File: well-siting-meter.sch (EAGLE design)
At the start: 27 parts, among them J2 7805

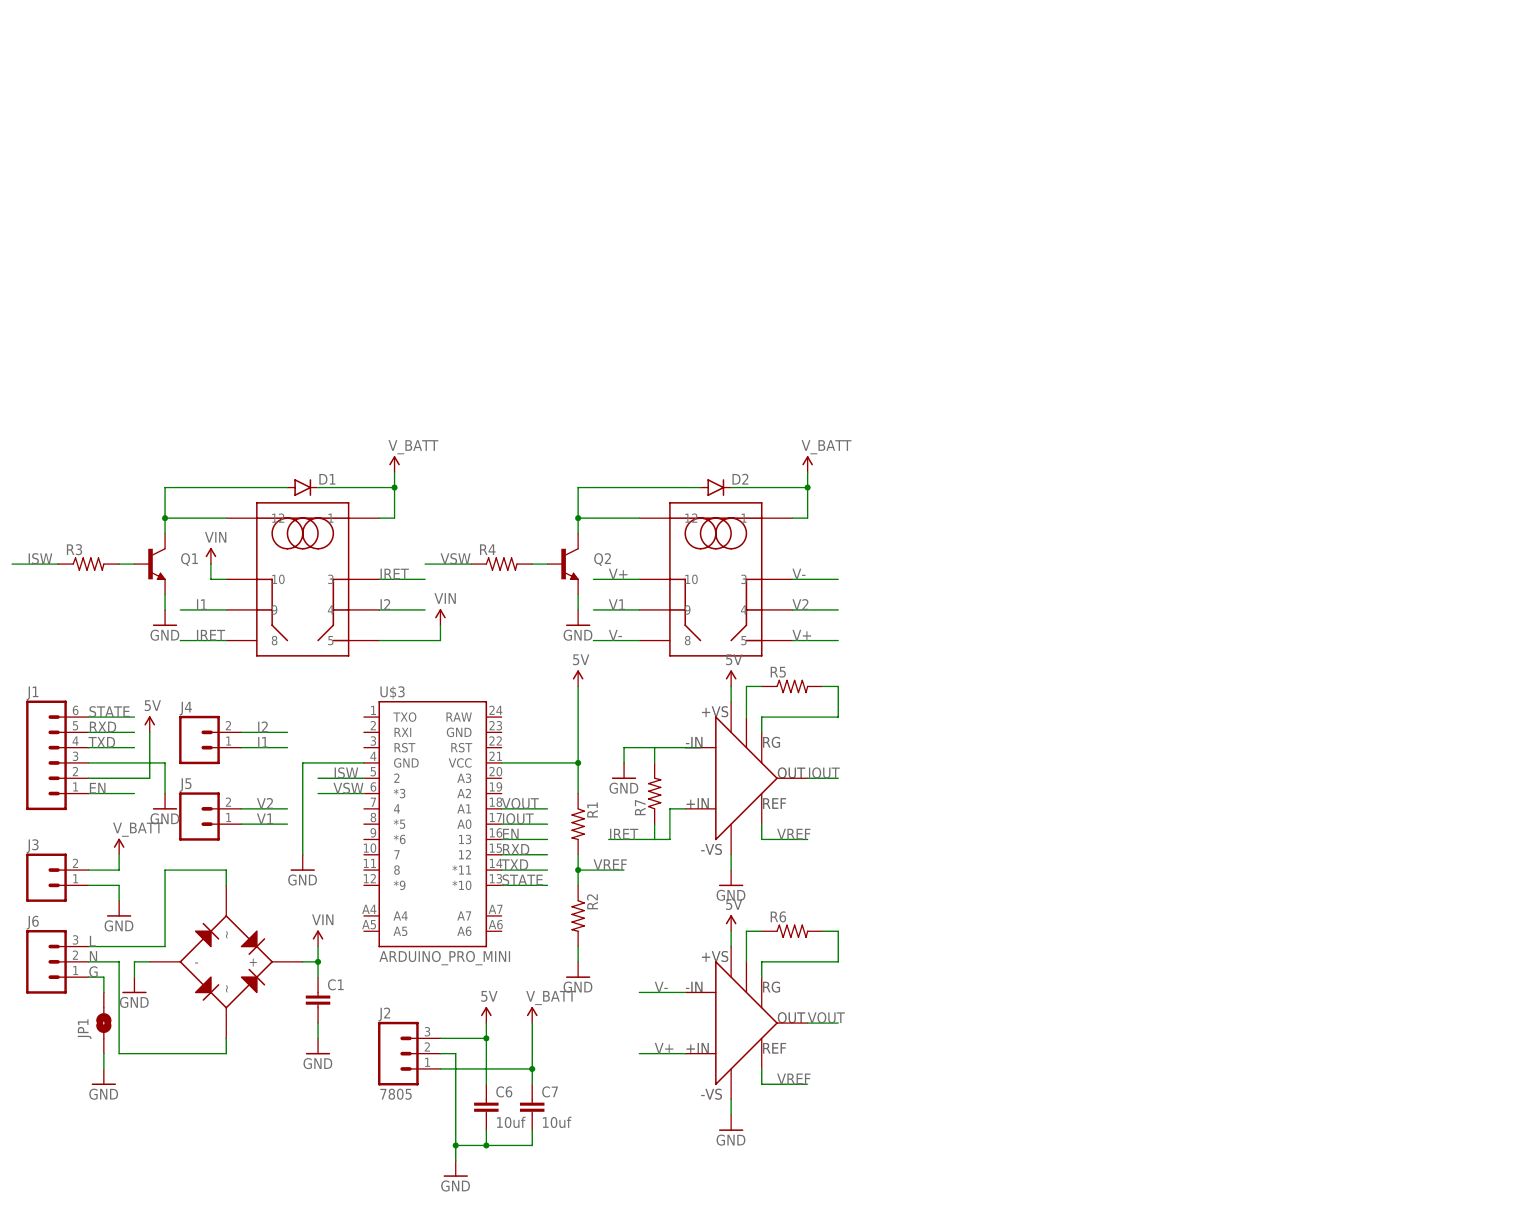
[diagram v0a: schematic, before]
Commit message: boost circuit, lcd screen, starting board layout
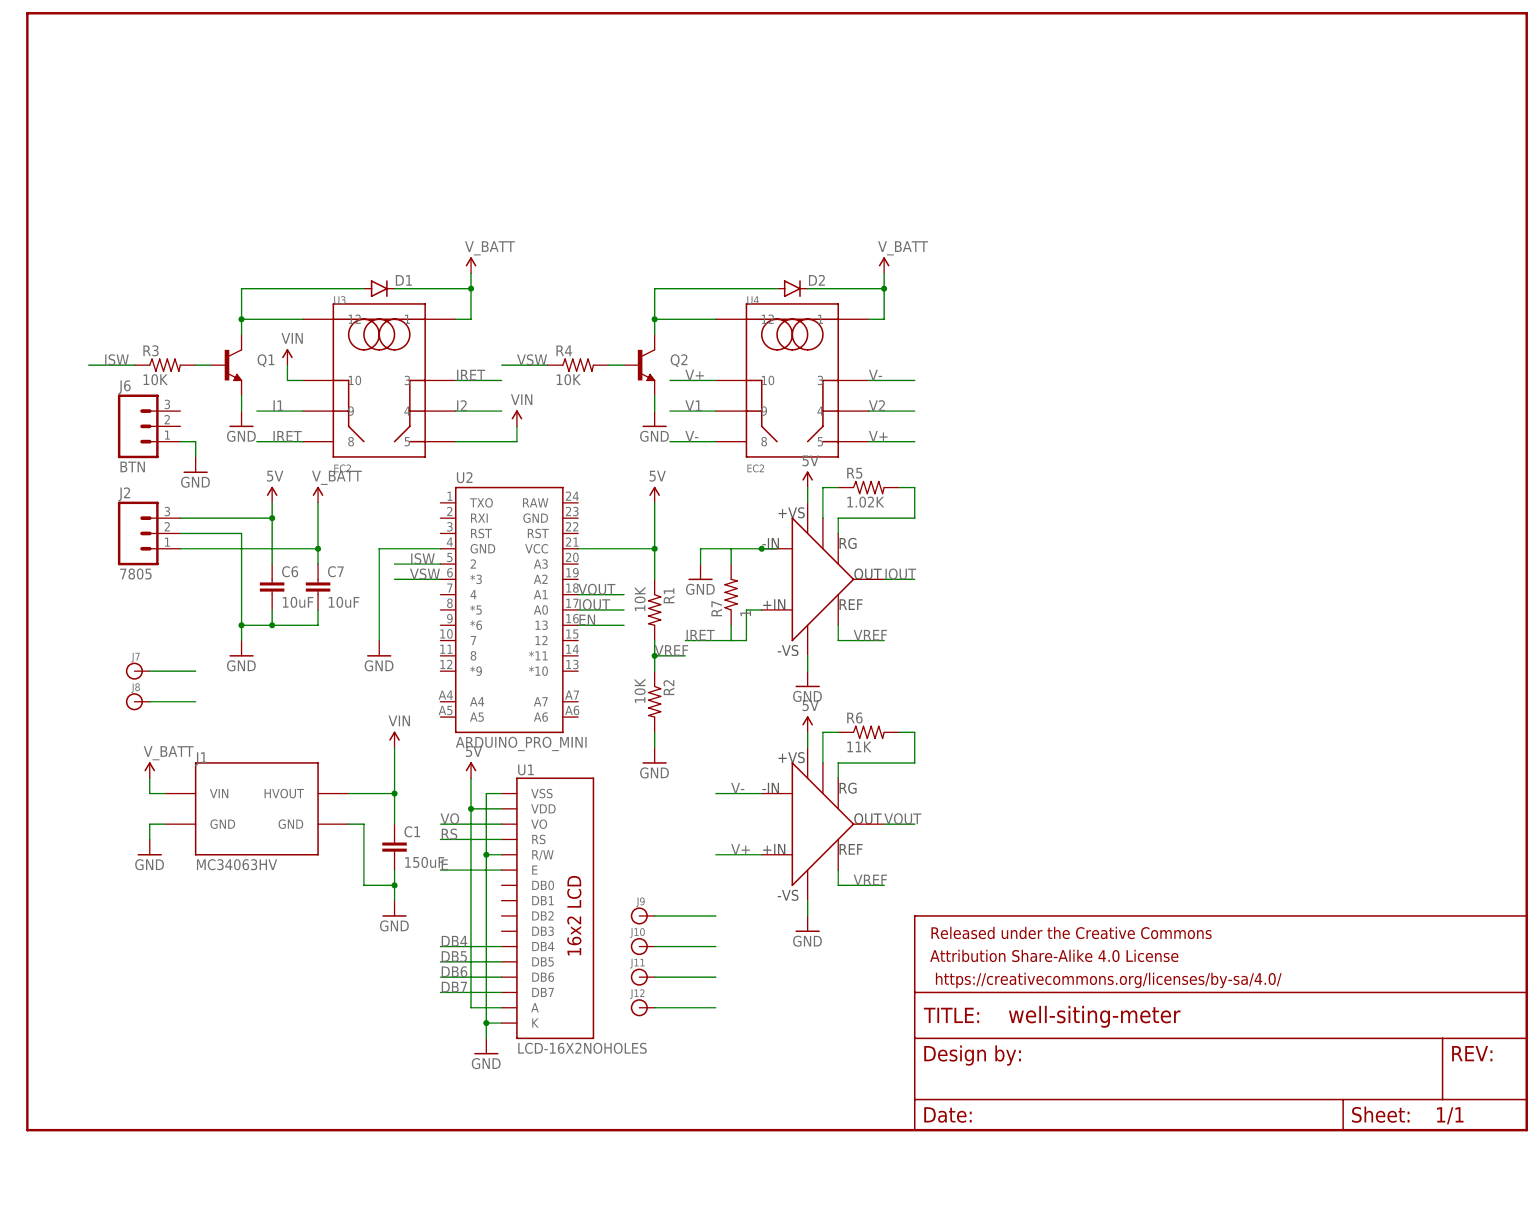
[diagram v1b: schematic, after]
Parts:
- removed J3, J4, J5: (no value), SparkFun-Connectors:M025MM
- removed JP1: JUMPER-PAD-2-NO, SparkFun-Passives:JUMPER-PAD-2-NO
- removed U$1, U$2: EC2, ec2:EC2
- removed U$3: ARDUINO_PRO_MINI, SparkFun-Boards:ARDUINO_PRO_MINI
- removed U$4, U$5: AD623, ad623:AD623
- removed U$6: DF2X, df2x:DF2X
- added FRAME1: FRAME-LETTER, SparkFun-Aesthetics:FRAME-LETTER
- added J10, J11, J12, J7, J8, J9: (no value), SparkFun-Connectors:BANANA_CONN
- added U1: LCD-16X2NOHOLES, SparkFun-Displays:LCD-16X2NOHOLES
- added U2: ARDUINO_PRO_MINI, SparkFun-Boards:ARDUINO_PRO_MINI
- added U3, U4: EC2, ec2:EC2
- added U5, U6: AD623, ad623:AD623
- C1: value (none) -> 150uF
- C6, C7: value 10uf -> 10uF
- J1: value (none) -> MC34063HV; device SparkFun-Connectors:M06SILK_FEMALE_PTH -> mc34063hv:MC34063HV
- J6: value (none) -> BTN; device SparkFun-Connectors:M03-SCREW-5MM -> SparkFun-Connectors:M03PTH; PN (none) -> 811-2196-5-ND; PN2 (none) -> LM7805CT-ND
- R1, R2, R3, R4: value (none) -> 10K
- R5: value (none) -> 1.02K
- R6: value (none) -> 11K
- R7: value (none) -> 1
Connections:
- removed net G: J6.1, JP1.2
- removed net L: J6.3, U$6.~@2
- removed net N: J6.2, U$6.~@3
- removed net RXD: J1.5, U$3.12
- removed net STATE: J1.6, U$3.*10
- removed net TXD: J1.4, U$3.*11
- new net DB4: U1.DB4
- new net DB5: U1.DB5
- new net DB6: U1.DB6
- new net DB7: U1.DB7
- new net E: U1.E
- new net RS: U1.RS
- new net VO: U1.VO
- net 5V: now also U1.A, U1.VDD, U2.VCC, U5.+VS, U6.+VS; no longer J1.2, U$3.VCC, U$4.+VS, U$5.+VS
- net EN: now also U2.13; no longer J1.1, U$3.13
- net GND: now also J1.GND@2, J1.GND@4, J6.1, J8.1, U1.K, U1.R/W, U1.VSS, U2.GND, U5.-IN, U5.-VS, U6.-VS; no longer J1.3, J3.1, JP1.1, U$3.GND, U$4.-VS, U$5.-VS, U$6.-
- net I1: now also J9.1, U3.9; no longer J4.1, U$1.9
- net I2: now also J10.1, U3.4; no longer J4.2, U$1.4
- net IOUT: now also U2.A0, U5.OUT; no longer U$3.A0, U$4.OUT
- net IRET: now also U3.3, U3.8, U5.+IN; no longer U$1.3, U$1.8, U$4.+IN
- net ISW: now also U2.2; no longer U$3.2
- net N$1: now also U4.12; no longer U$2.12
- net N$24: now also U5.-RG; no longer U$4.-RG
- net N$25: now also U5.+RG; no longer U$4.+RG
- net N$26: now also U6.-RG; no longer U$5.-RG
- net N$27: now also U6.+RG; no longer U$5.+RG
- net N$4: now also U3.12; no longer U$1.12
- net V+: now also U4.10, U4.5, U6.+IN; no longer U$2.10, U$2.5, U$5.+IN
- net V-: now also U4.3, U4.8, U6.-IN; no longer U$2.3, U$2.8, U$5.-IN
- net V1: now also J11.1, U4.9; no longer J5.1, U$2.9
- net V2: now also J12.1, U4.4; no longer J5.2, U$2.4
- net VIN: now also J1.HVOUT, U3.10, U3.5; no longer U$1.10, U$1.5, U$6.+
- net VOUT: now also U2.A1, U6.OUT; no longer U$3.A1, U$5.OUT
- net VREF: now also U5.REF, U6.REF; no longer U$4.REF, U$5.REF
- net VSW: now also U2.*3; no longer U$3.*3
- net V_BATT: now also J1.VIN, J7.1, U3.1, U4.1; no longer J3.2, U$1.1, U$2.1
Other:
- moved on the sheet: C1, C6, C7, D1, D2, J2, J6, Q1, Q2, R1, R2, R3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

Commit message: "finished" design, but need to update boot circuity for > 10W max
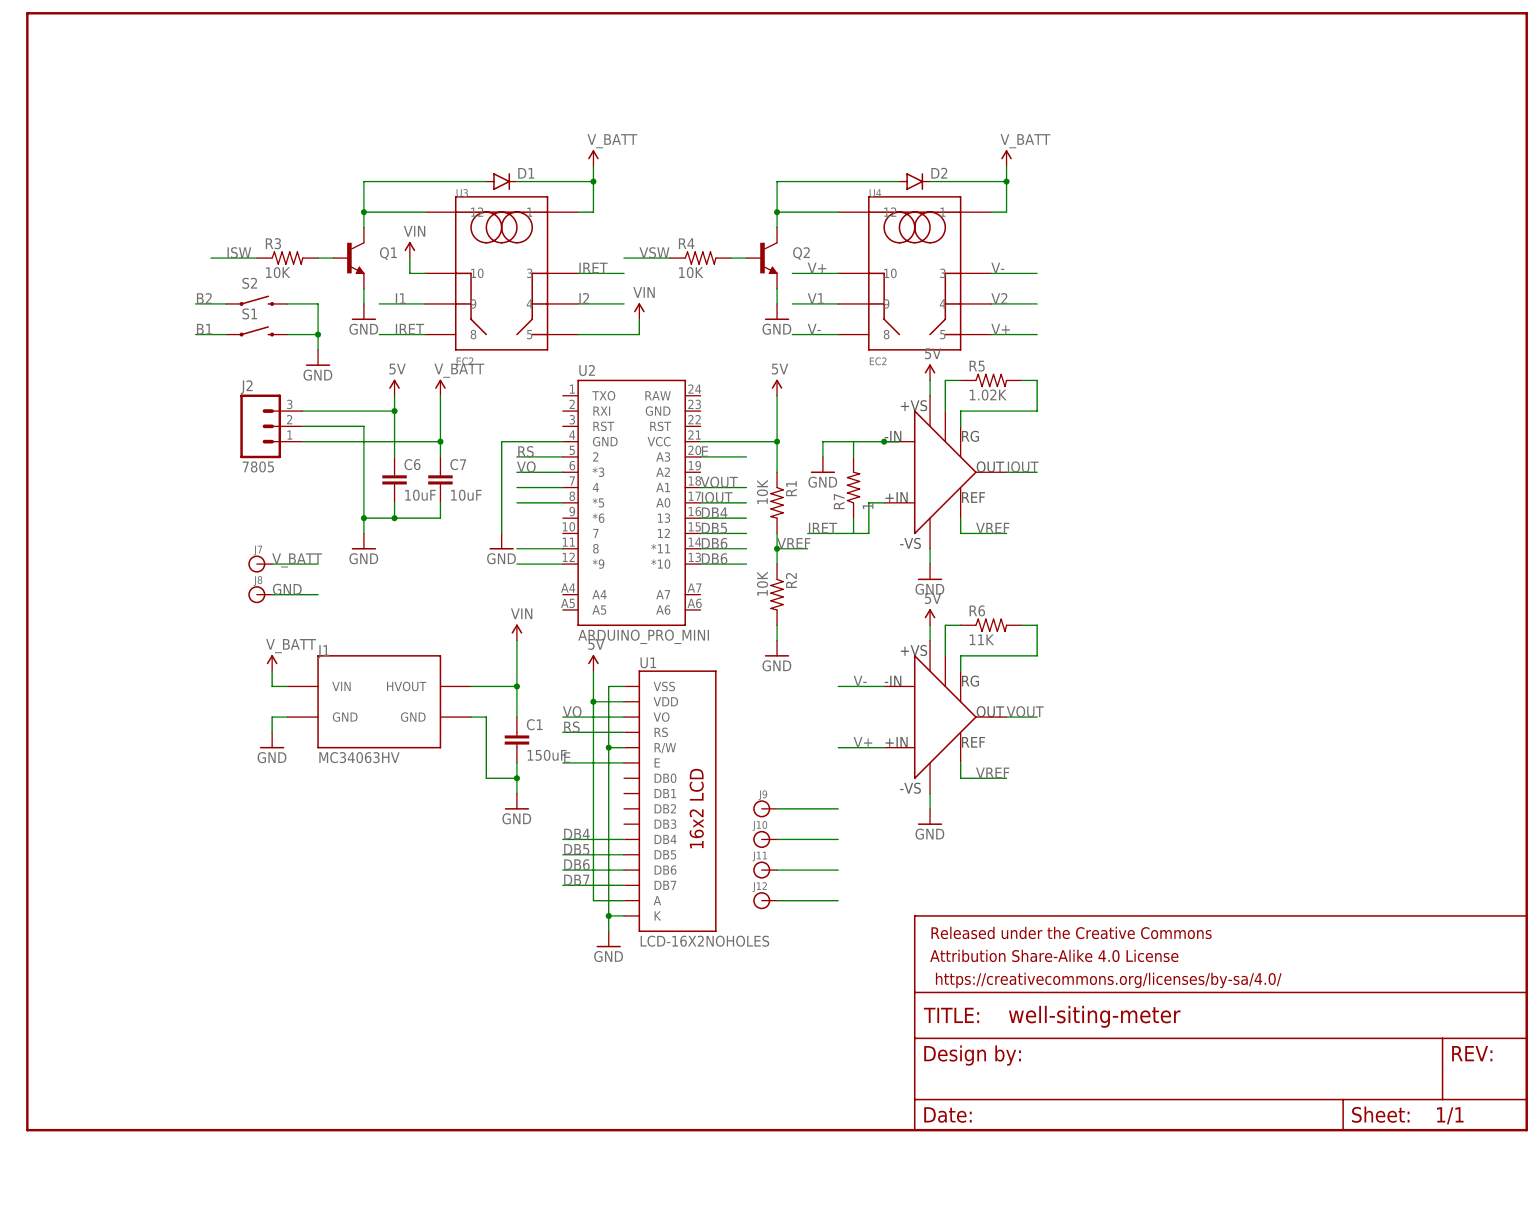
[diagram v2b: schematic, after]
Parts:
- removed J6: BTN, SparkFun-Connectors:M03PTH
- added S1, S2: SWITCH-MOMENTARY-2PTH, SparkFun-Electromechanical:SWITCH-MOMENTARY-2PTH
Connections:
- removed net EN: U2.13
- new net B1: S1.1, U2.4
- new net B2: S2.1, U2.*5
- net DB4: now also U2.13
- net DB5: now also U2.12
- net DB6: now also U2.*11
- net DB7: now also U2.*10
- net E: now also U2.A3
- net GND: now also S1.2, S2.2; no longer J6.1
- net ISW: now also U2.8; no longer U2.2
- net RS: now also U2.2
- net VO: now also U2.*3
- net VSW: now also U2.*9; no longer U2.*3
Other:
- moved on the sheet: C1, C6, C7, D1, D2, J1, J10, J11, J12, J2, J7, J8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

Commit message: added boost circuit
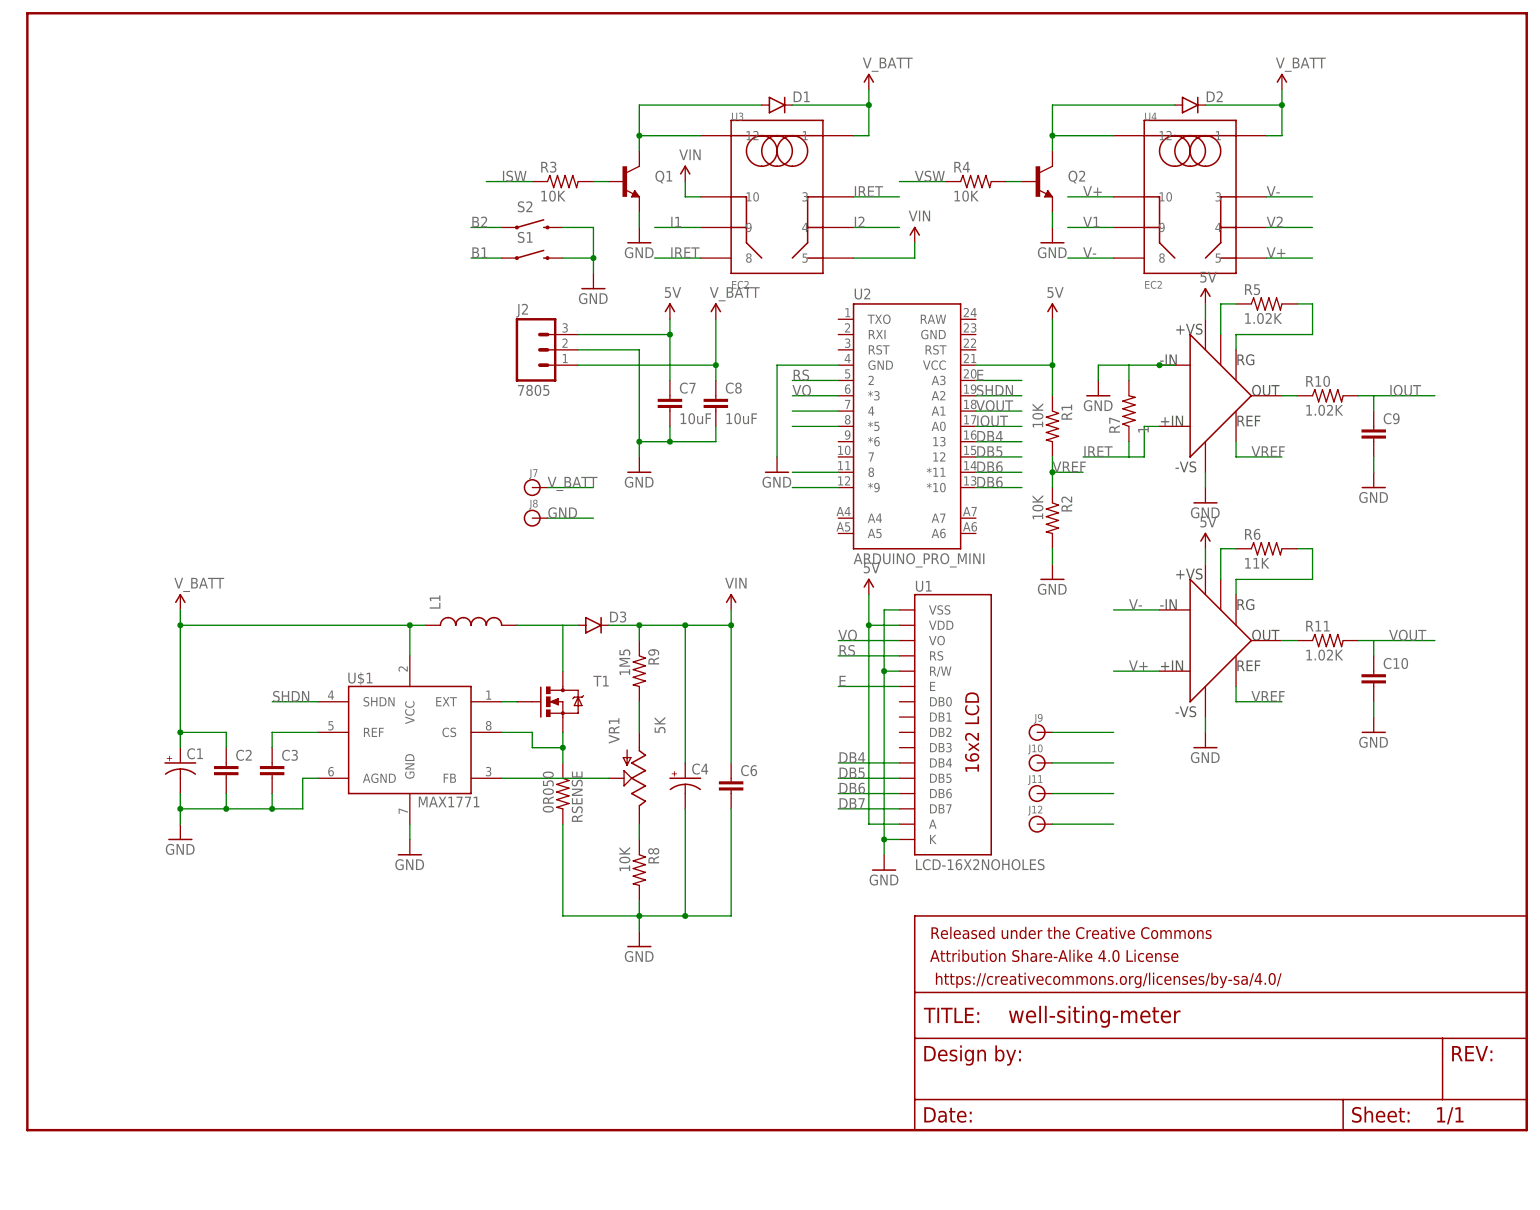
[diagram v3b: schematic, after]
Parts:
- removed J1: MC34063HV, mc34063hv:MC34063HV
- added C10, C2, C3, C9: (no value), SparkFun-Passives:CAPPTH
- added C4: (no value), SparkFun-Passives:CAP_POLPTH1
- added C8: 10uF, SparkFun-Passives:CAPPTH
- added D3: (no value), SparkFun-DiscreteSemi:DIODEPTH
- added L1: (no value), SparkFun-Passives:INDUCTORRLB0912
- added R10, R11: 1.02K, SparkFun-Passives:RESISTORPTH-1/4W
- added R8: 10K, SparkFun-Passives:RESISTORPTH-1/4W
- added R9: 1M5, SparkFun-Passives:RESISTORPTH-1/4W
- added RSENSE: 0R050, SparkFun-Passives:RESISTORPTH-1/4W
- added T1: MOSFET-NCHANNELFQP30N06L, SparkFun-DiscreteSemi:MOSFET-NCHANNELFQP30N06L
- added U$1: MAX1771, max1771:MAX1771
- added VR1: 5K, SparkFun-Electromechanical:POTTRIM
- C1: value 150uF -> (none); device SparkFun-Passives:CAPPTH3 -> SparkFun-Passives:CAP_POLPTH1
- C6: value 10uF -> (none); PN 490-7202-1-ND -> (none)
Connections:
- new net N$10: T1.G, U$1.EXT
- new net N$11: RSENSE.1, T1.S, U$1.CS
- new net N$12: R10.1, U5.OUT
- new net N$14: R11.1, U6.OUT
- new net N$15: U$1.FB, VR1.S
- new net N$6: R9.2, VR1.A
- new net N$7: C3.1, U$1.REF
- new net N$8: R8.1, VR1.E
- new net N$9: D3.A, L1.2, T1.D
- new net SHDN: U$1.SHDN, U2.A2
- net 5V: now also C7.1; no longer C6.1
- net GND: now also C1.-, C10.2, C2.2, C3.2, C4.-, C8.2, C9.2, R8.2, RSENSE.2, U$1.AGND, U$1.GND; no longer C1.2, J1.GND@2, J1.GND@4
- net IOUT: now also C9.1, R10.2; no longer U5.OUT
- net VIN: now also C4.+, C6.1, D3.C, R9.1; no longer C1.1, J1.HVOUT
- net VOUT: now also C10.1, R11.2; no longer U6.OUT
- net V_BATT: now also C1.+, C2.1, C8.1, L1.1, U$1.VCC; no longer C7.1, J1.VIN
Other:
- moved on the sheet: C6, C7, D1, D2, J10, J11, J12, J2, J7, J8, J9, Q1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
